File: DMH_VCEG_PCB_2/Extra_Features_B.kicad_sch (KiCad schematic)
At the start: 46 parts, among them J25 Conn_01x10_PinHeader, J26 Conn_01x10_PinHeader, Q8 BC548, SW2 SW_DPDT_x2, SW5 SW_SPDT_321_OnOff, U10 TL074, U12 40106, U17 TL074, U20 4001

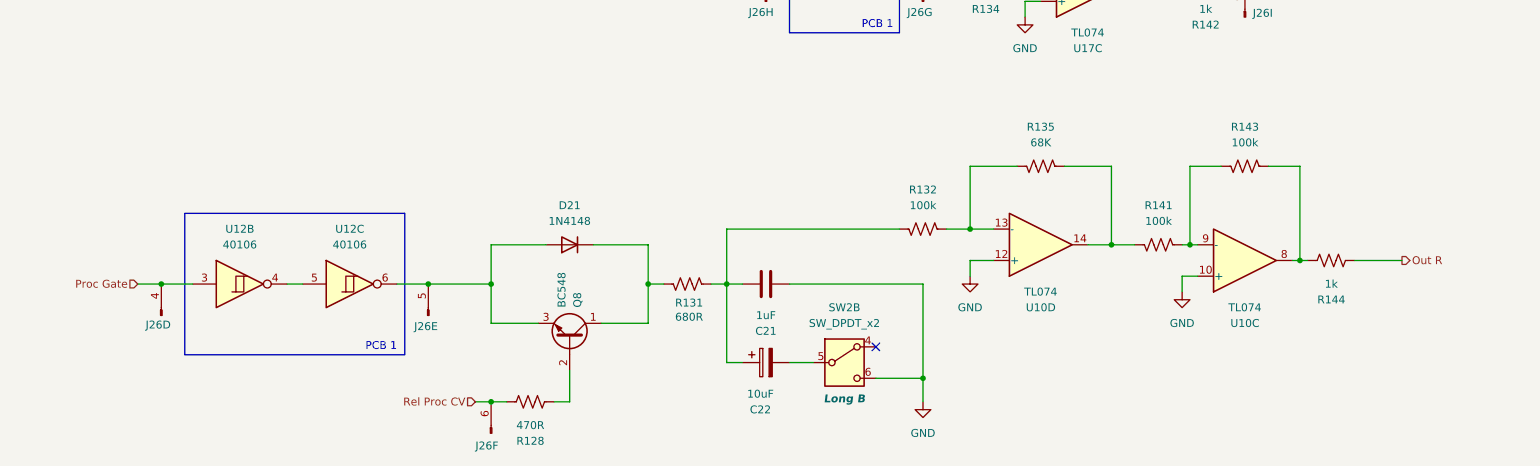
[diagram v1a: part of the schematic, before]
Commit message: Placed ICs and pin headers on PCB 2
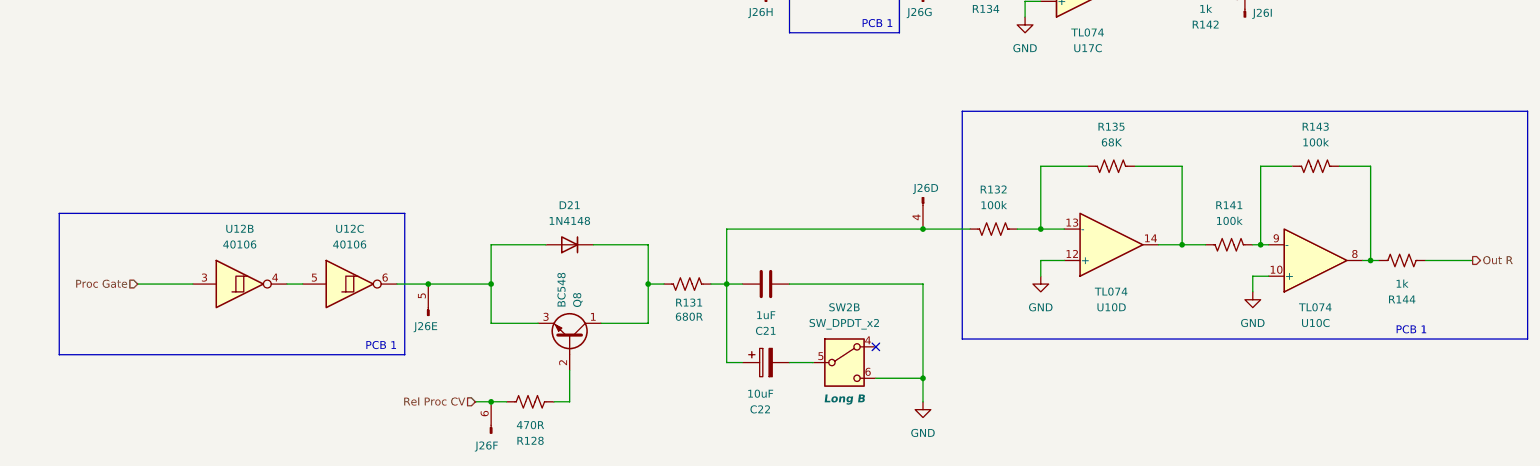
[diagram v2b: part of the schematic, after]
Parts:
- J25, J26: footprint (none) -> Connector_PinSocket_2.54mm:PinSocket_1x10_P2.54mm_Vertical
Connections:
- net Proc Gate: no longer J26.4 (Pin_4)
- net at C21.1, C22.1, R131.1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: now also J26.4 (Pin_4)
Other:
- moved on the sheet: R132, R135, R141, R143, R144, U10C, U10D

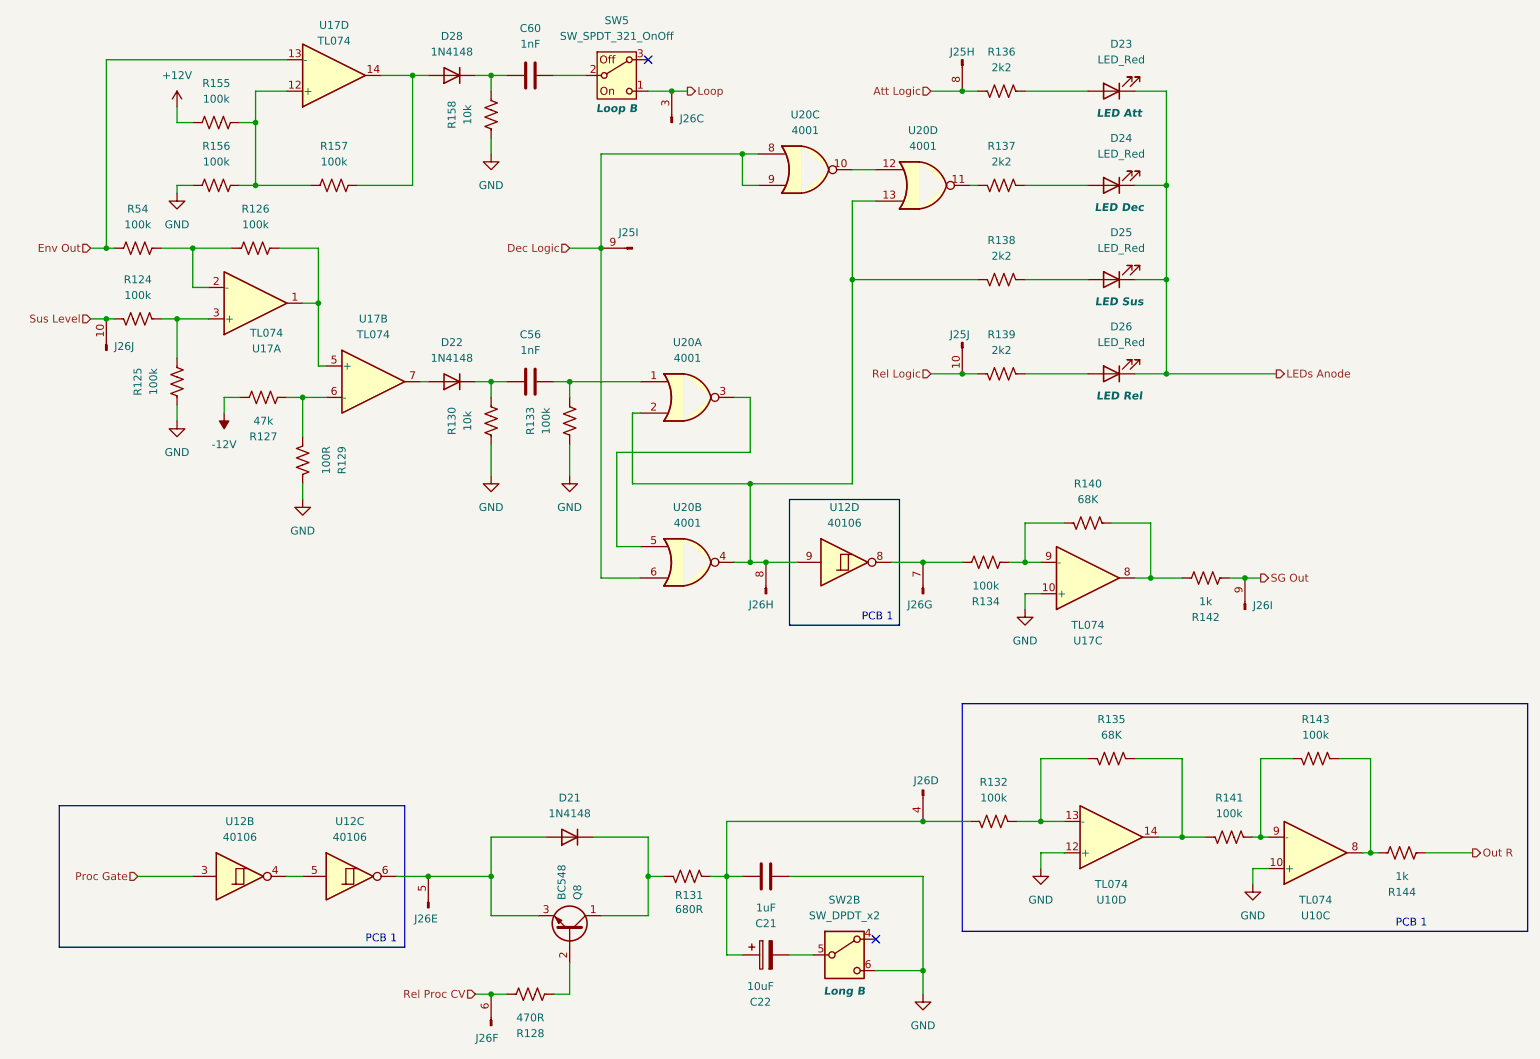
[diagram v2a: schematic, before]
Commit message: Addition of manual gate ongoing
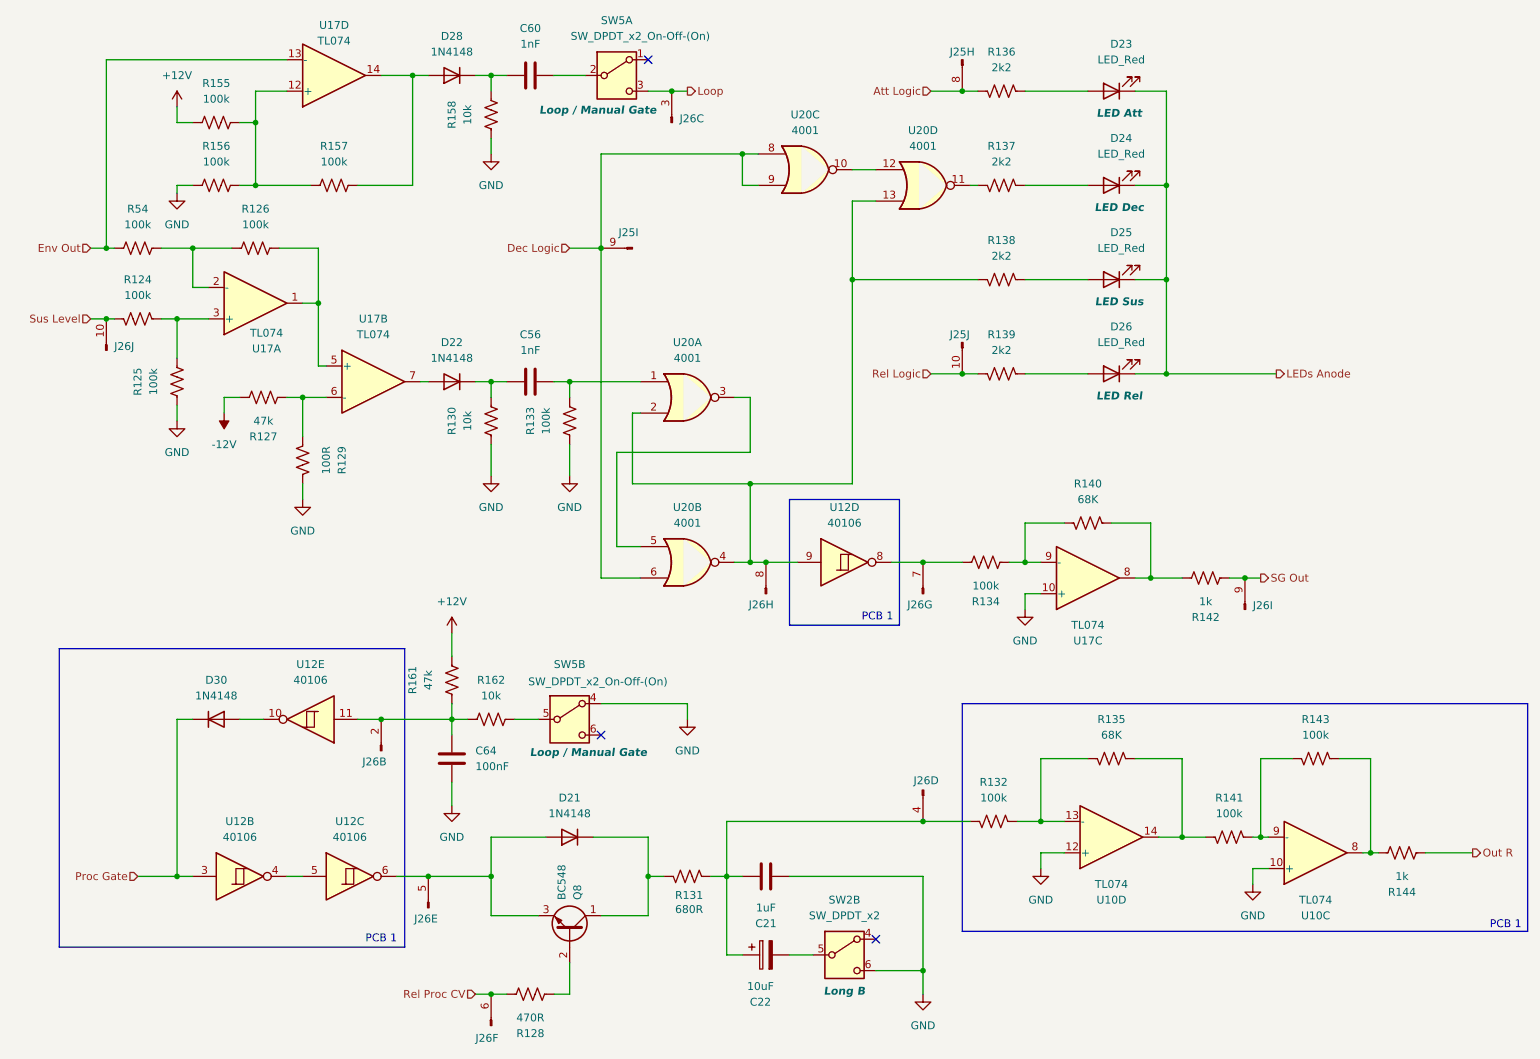
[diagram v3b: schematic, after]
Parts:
- removed SW5: SW_SPDT_321_OnOff, SynthStuff:Toggle_Switch_TE, symbol SynthStuff:SW_SPDT_321_OnOff
- added C64: 100nF, Capacitor_THT:C_Disc_D4.3mm_W1.9mm_P5.00mm, symbol Device:C
- added D30: 1N4148, Diode_THT:D_DO-35_SOD27_P7.62mm_Horizontal, symbol Diode:1N4148
- added unit 2 of J26
- added R161: 47k, Resistor_THT:R_Axial_DIN0207_L6.3mm_D2.5mm_P7.62mm_Horizontal, symbol Device:R_US
- added R162: 10k, Resistor_THT:R_Axial_DIN0207_L6.3mm_D2.5mm_P7.62mm_Horizontal, symbol Device:R_US
- added SW5: SW_DPDT_x2_On-Off-(On), symbol Switch:SW_DPDT_x2
- added unit 5 of U12
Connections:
- net +12V: now also R161.1
- net GND: now also C64.2, SW5.4 (A)
- net Loop: now also SW5.3 (C)
- net Proc Gate: now also D30.1 (K)
- net at C60.2: now also SW5.2 (B)
- new net: R162.1, SW5.5 (B)
- new net: C64.1, J26.2 (Pin_2), R161.2, R162.2, U12.11
- new net: D30.2 (A), U12.10
- no-connect marks 2 -> 3

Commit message: Copied Manual Gate circuit to PCB 1 schematic
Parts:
- SW5: footprint (none) -> SynthStuff:Toggle_Switch_2_Poles_TE
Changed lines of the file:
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@@
 			)
 		)
-		(property "Footprint" ""
+		(property "Footprint" "SynthStuff:Toggle_Switch_2_Poles_TE"
 			(at 101.6 127 0)
 			(effects
@@
 			)
 		)
-		(property "Footprint" ""
+		(property "Footprint" "SynthStuff:Toggle_Switch_2_Poles_TE"
 			(at 109.22 22.86 0)
 			(effects

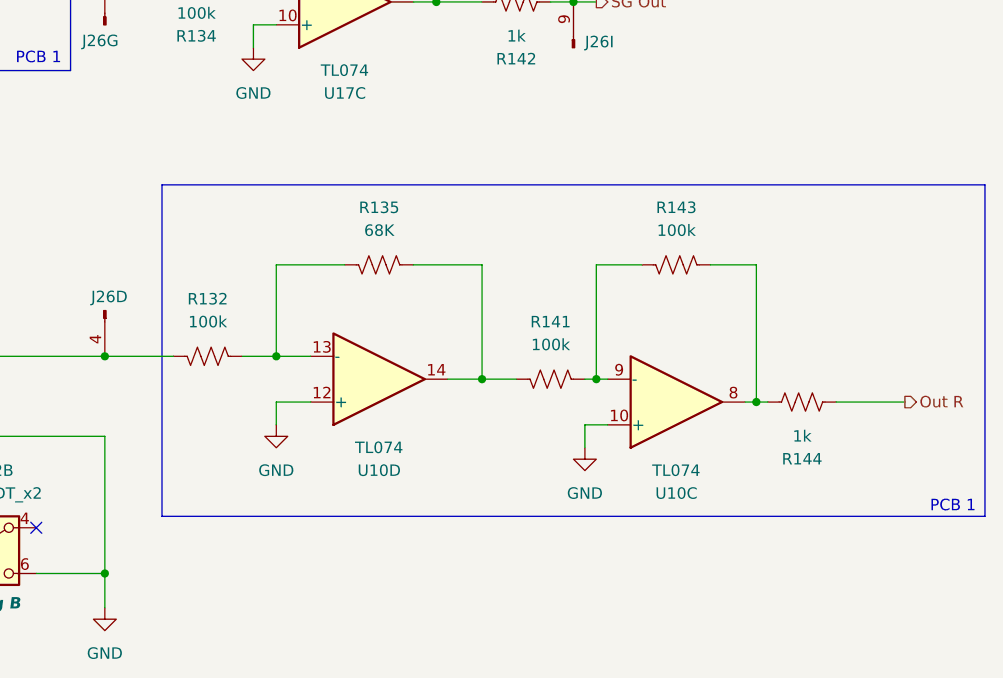
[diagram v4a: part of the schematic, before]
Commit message: Added Output attenuation circuit
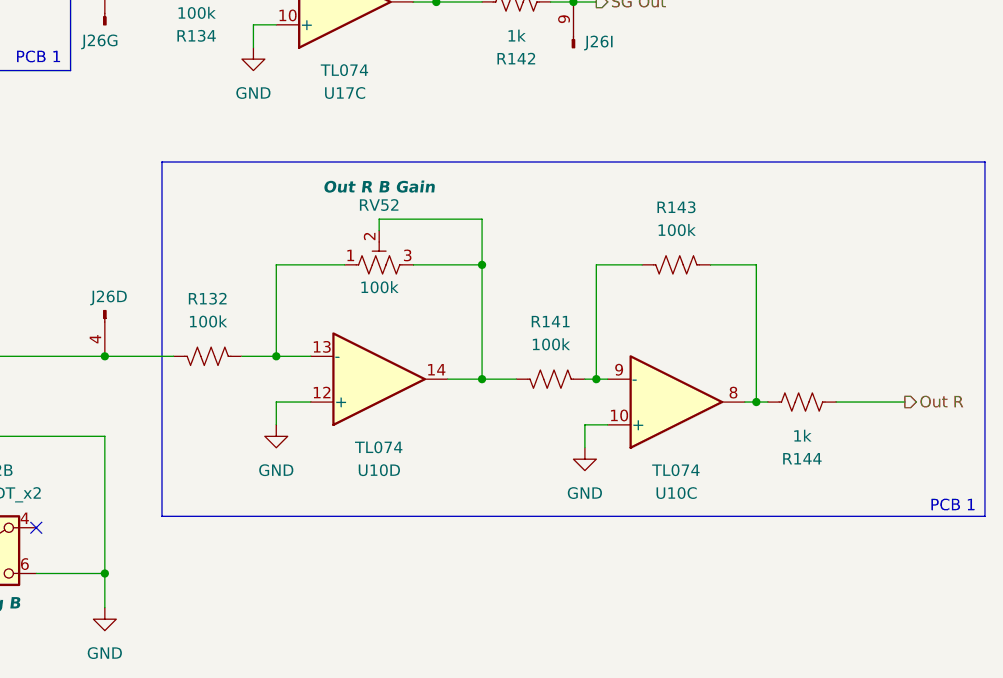
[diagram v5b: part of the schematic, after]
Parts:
- removed R135: 68K, Resistor_THT:R_Axial_DIN0207_L6.3mm_D2.5mm_P7.62mm_Horizontal, symbol Device:R_US
- added RV52: 100k, Potentiometer_THT:Potentiometer_Bourns_3296X_Horizontal, symbol Device:R_Potentiometer_Trim_US
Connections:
- net at R132.2, U10.13 (-): now also RV52.1
- net at R141.1, U10.14: now also RV52.2, RV52.3
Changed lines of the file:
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@@
 	)
 	(rectangle
-		(start 165.1 124.46)
+		(start 165.1 121.92)
 		(end 256.54 161.29)
 		(stroke
@@
 	)
 	(junction
+		(at 200.66 133.35)
+		(diameter 0)
+		(color 0 0 0 0)
+	)
+	(junction
 		(at 158.75 101.6)
 		(diameter 0)
@@
 	(wire
 		(pts
+			(xy 200.66 128.27) (xy 200.66 133.35)
+		)
+		(stroke
+			(width 0)
+			(type default)
+		)
+	)
+	(wire
+		(pts
 			(xy 88.9 72.39) (xy 91.44 72.39)
 		)
@@
 	(wire
 		(pts
+			(xy 189.23 129.54) (xy 189.23 128.27)
+		)
+		(stroke
+			(width 0)
+			(type default)
+		)
+	)
+	(wire
+		(pts
 			(xy 82.55 127) (xy 82.55 129.54)
 		)
@@
 	(wire
 		(pts
+			(xy 189.23 128.27) (xy 200.66 128.27)
+		)
+		(stroke
+			(width 0)
+			(type default)
+		)
+	)
+	(wire
+		(pts
 			(xy 175.26 25.4) (xy 185.42 25.4)
 		)
@@
 	)
 	(symbol
-		(lib_id "Device:R_US")
-		(at 189.23 133.35 90)
-		(mirror x)
-		(unit 1)
-		(exclude_from_sim no)
-		(in_bom yes)
-		(on_board no)
-		(dnp no)
-		(property "Reference" "R135"
-			(at 189.23 127 90)
-			(effects
-				(font
-					(size 1.27 1.27)
-				)
-			)
-		)
-		(property "Value" "68K"
-			(at 189.23 129.54 90)
-			(effects
-				(font
-					(size 1.27 1.27)
-				)
-			)
-		)
-		(property "Footprint" "Resistor_THT:R_Axial_DIN0207_L6.3mm_D2.5mm_P7.62mm_Horizontal"
-			(at 189.484 134.366 90)
-			(effects
-				(font
-					(size 1.27 1.27)
-				)
-				(hide yes)
-			)
-		)
-		(property "Datasheet" "~"
-			(at 189.23 133.35 0)
-			(effects
-				(font
-					(size 1.27 1.27)
-				)
-				(hide yes)
-			)
-		)
-		(property "Description" "Resistor, US symbol"
-			(at 189.23 133.35 0)
-			(effects
-				(font
-					(size 1.27 1.27)
-				)
-				(hide yes)
-			)
-		)
-		(pin "2"
-		)
-		(pin "1"
-		)
-		(instances
-			(project "DMH_VCEG_PCB_1"
-				(path "/58f4306d-5387-4983-bb08-41a2313fd315/5112ef52-02ff-4071-9179-b1c0d55d0b73"
-					(reference "R135")
-					(unit 1)
-				)
-			)
-		)
-	)
-	(symbol
 		(lib_id "SynthStuff:Conn_01x10_PinHeader")
 		(at 133.35 106.68 90)
@@
 				)
 			)
+		)
+	)
+	(symbol
+		(lib_id "Device:R_Potentiometer_Trim_US")
+		(at 189.23 133.35 90)
+		(unit 1)
+		(exclude_from_sim no)
+		(in_bom yes)
+		(on_board no)
+		(dnp no)
+		(property "Reference" "RV52"
+			(at 189.23 126.746 90)
+			(effects
+				(font
+					(size 1.27 1.27)
+				)
+			)
+		)
+		(property "Value" "100k"
+			(at 189.23 135.89 90)
+			(effects
+				(font
+					(size 1.27 1.27)
+				)
+			)
+		)
+		(property "Footprint" "Potentiometer_THT:Potentiometer_Bourns_3296X_Horizontal"
+			(at 189.23 133.35 0)
+			(effects
+				(font
+					(size 1.27 1.27)
+				)
+				(hide yes)
+			)
+		)
+		(property "Datasheet" "~"
+			(at 189.23 133.35 0)
+			(effects
+				(font
+					(size 1.27 1.27)
+				)
+				(hide yes)
+			)
+		)
+		(property "Description" "Trim-potentiometer, US symbol"
+			(at 189.23 133.35 0)
+			(effects
+				(font
+					(size 1.27 1.27)
+				)
+				(hide yes)
+			)
+		)
+		(property "Function" "Out R B Gain"
+			(at 189.23 124.714 90)
+			(effects
+				(font
+					(size 1.27 1.27)
+					(thickness 0.254)
+					(bold yes)
+					(italic yes)
+				)
+			)
+		)
+		(pin "2"
+		)
+		(pin "1"
+		)
+		(pin "3"
+		)
+		(instances
+			(project "DMH_VCEG_PCB_2"
+				(path "/58f4306d-5387-4983-bb08-41a2313fd315/5112ef52-02ff-4071-9179-b1c0d55d0b73"
+					(reference "RV52")
+					(unit 1)
+				)
+			)
